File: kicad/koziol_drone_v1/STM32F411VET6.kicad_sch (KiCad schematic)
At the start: 1 part, among them U1 STM32F411VET6

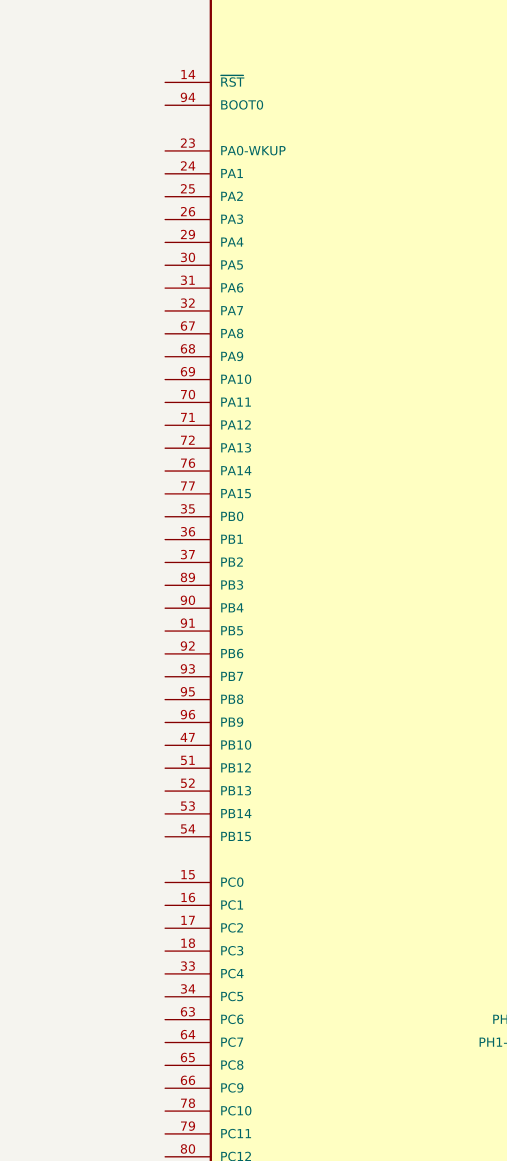
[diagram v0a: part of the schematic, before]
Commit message: mcu scheme + buses
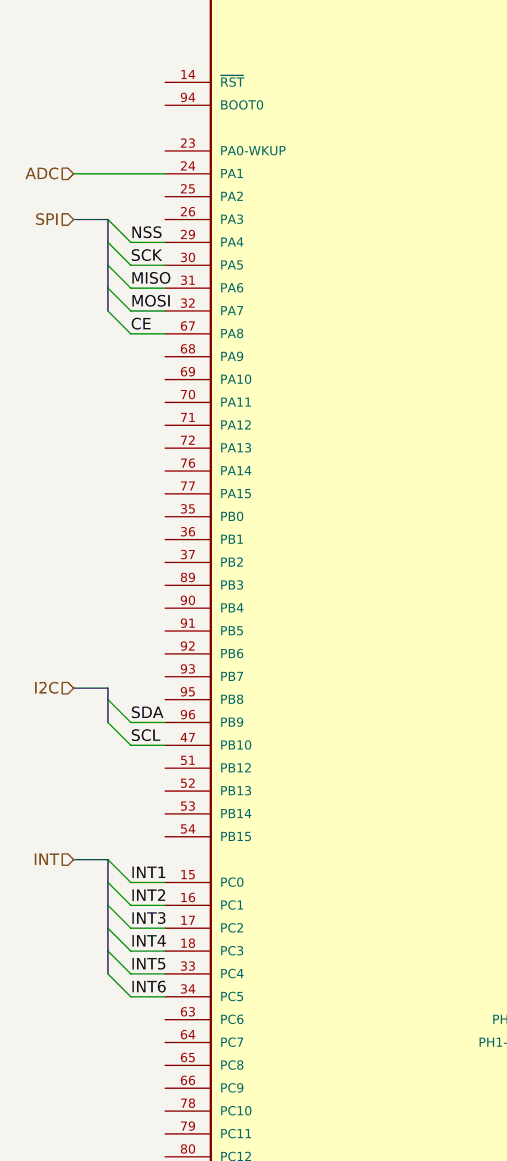
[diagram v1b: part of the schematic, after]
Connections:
- net INT1: now reaches U1.15 (PC0)
- net INT2: now reaches U1.16 (PC1)
- net INT3: now reaches U1.17 (PC2)
- net INT4: now reaches U1.18 (PC3)
- net ADC: now reaches U1.24 (PA1)
- net NSS: now reaches U1.29 (PA4)
- net SCK: now reaches U1.30 (PA5)
- net MISO: now reaches U1.31 (PA6)
- net MOSI: now reaches U1.32 (PA7)
- net INT5: now reaches U1.33 (PC4)
- net INT6: now reaches U1.34 (PC5)
- net SCL: now reaches U1.47 (PB10)
- net CE: now reaches U1.67 (PA8)
- net SDA: now reaches U1.96 (PB9)

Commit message: scheme descriptions and PDF plot
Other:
- note added: "Microcontroller and additional components"
- note added: "stm32f411vet6"
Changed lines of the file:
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@@
+		)
+	)
+	(text "Microcontroller and additional components"
+		(exclude_from_sim no)
+		(at 221.234 170.18 0)
+		(effects
+			(font
+				(size 2.54 2.54)
+			)
+		)
+	)
+	(text "stm32f411vet6"
+		(exclude_from_sim no)
+		(at 200.406 189.992 0)
+		(effects
+			(font
+				(size 2.54 2.54)
+			)
 		)
 	)
